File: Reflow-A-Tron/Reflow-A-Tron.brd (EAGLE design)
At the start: 97.8 x 62.2 mm, 40 parts, among them IC1 ATMEGA644-10PU, J2 HOT, J3 NEUTRAL, Q1 FOXSLF/200-20, Q2 BSS123, U2 L4941BDT-TRDPAK-3, U4 MAX6675

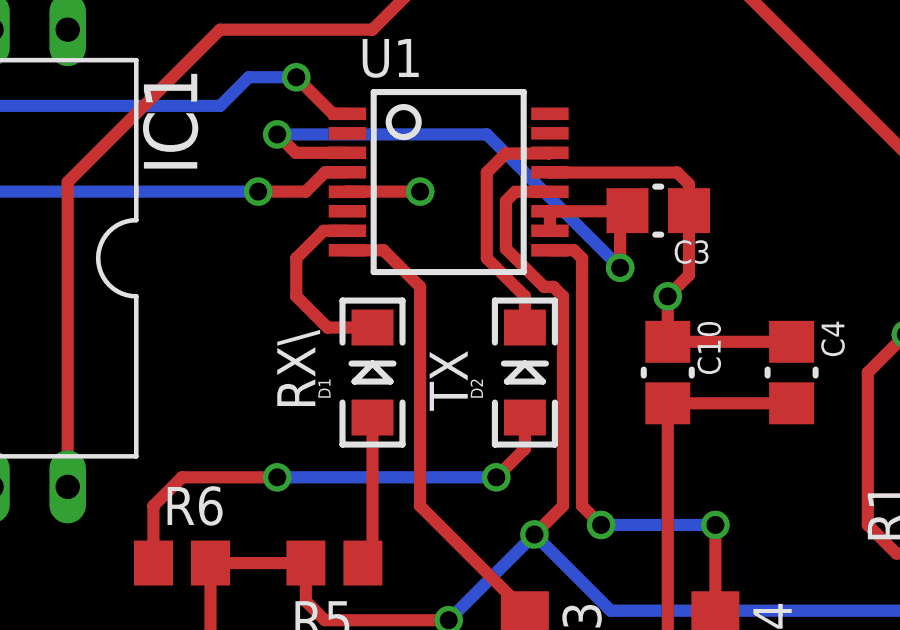
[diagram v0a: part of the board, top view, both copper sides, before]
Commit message: Only keep relevant data sheets
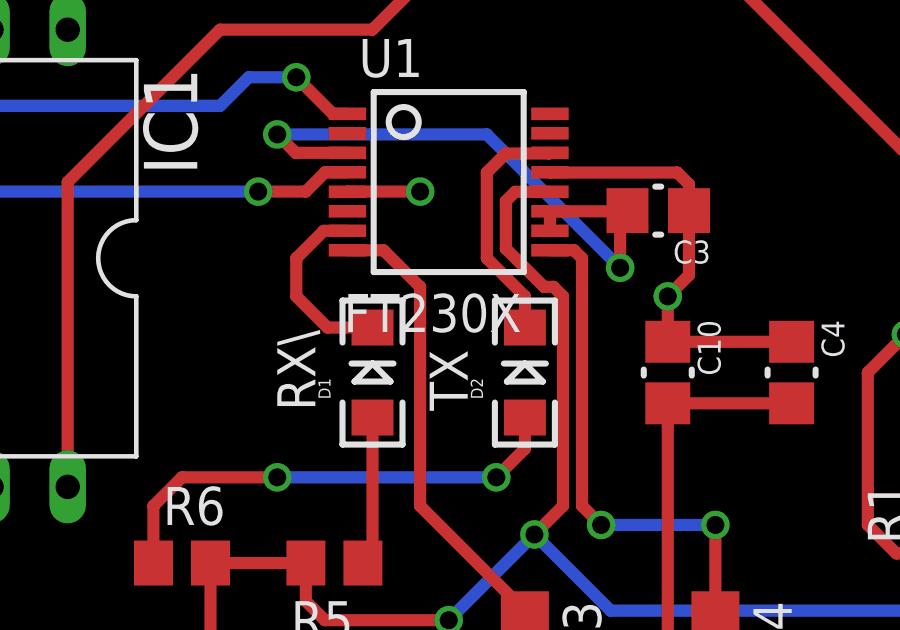
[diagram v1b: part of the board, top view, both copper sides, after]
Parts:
- U1: value (none) -> FT230X
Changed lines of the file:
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@@
 <attribute name="PROD_ID" value="CONN-08399" x="86.36" y="3.81" size="1.778" layer="27" display="off"/>
 </element>
-<element name="U1" library="neilbetham" package="SSOP-16" value="" x="64.77" y="27.94" rot="R270"/>
+<element name="U1" library="neilbetham" package="SSOP-16" value="FT230X" x="64.77" y="27.94" rot="R270"/>
 <element name="U2" library="neilbetham" package="DPAK" value="L4941BDT-TRDPAK-3" x="36.83" y="7.62" rot="R90"/>
 <element name="U4" library="SparkFun-AnalogIC" package="SOIC8" value="MAX6675" x="87.63" y="16.51">
